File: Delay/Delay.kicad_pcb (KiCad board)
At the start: 2 copper layers, 63 parts, among them J1 9V battery, J2 DC IN, J4 IN, J5 OUT, U1 PT2399, U2 LP2950-5.0_TO252, U3 TL072

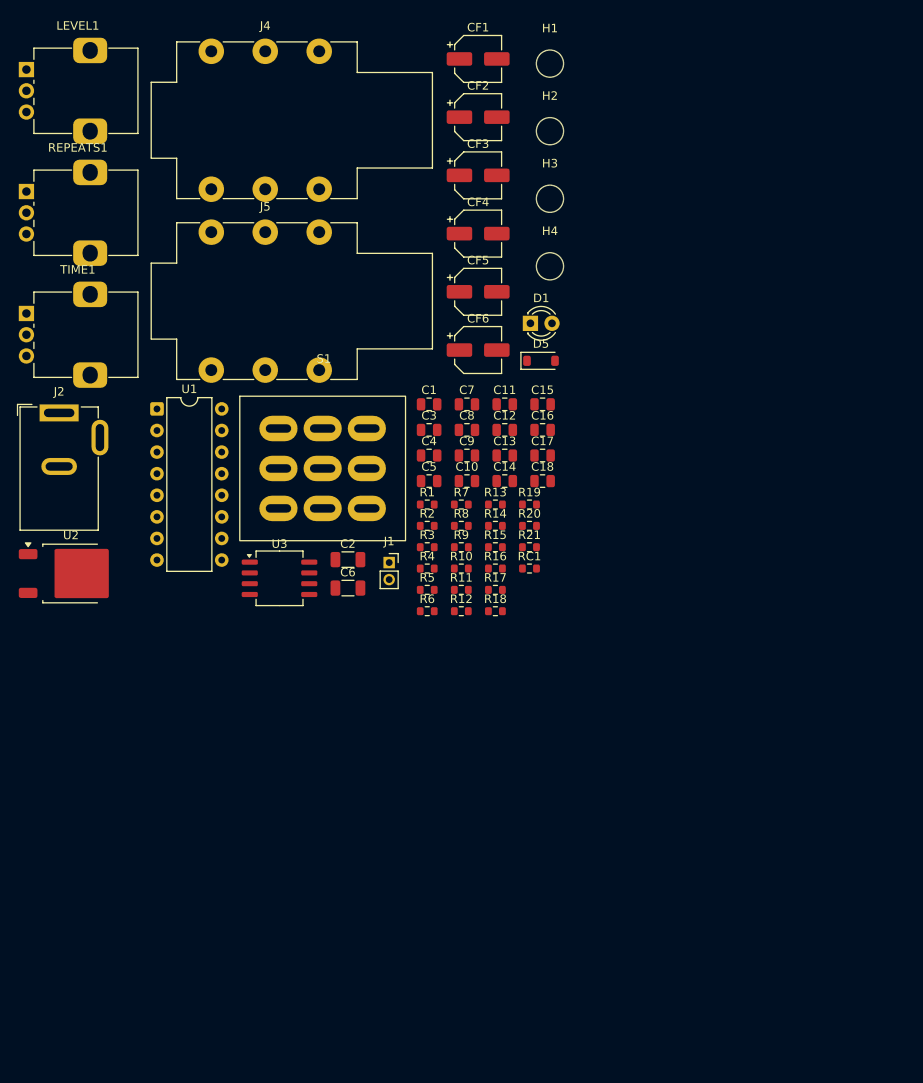
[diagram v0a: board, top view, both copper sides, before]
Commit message: Completed PCB layout, still need to finish BOM.
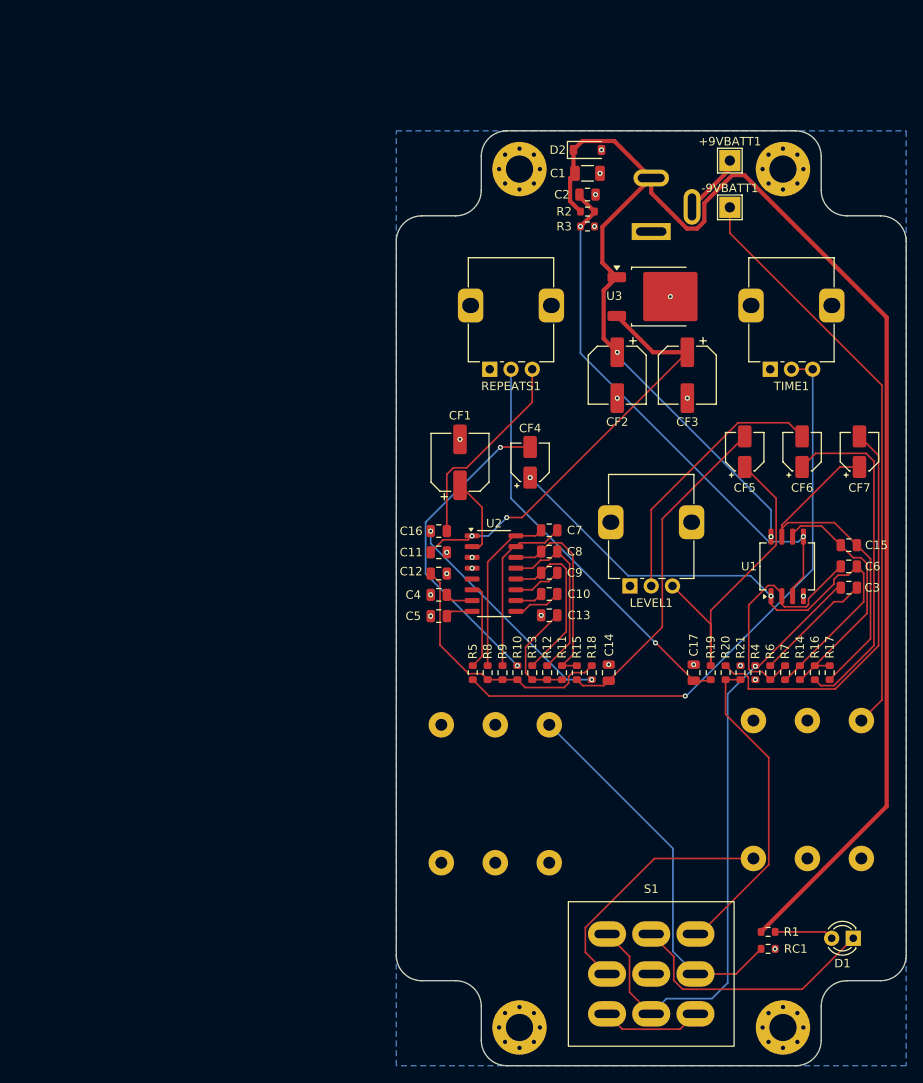
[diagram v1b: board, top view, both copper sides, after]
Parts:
- removed C18: 100pF, Capacitor_SMD:C_0805_2012Metric
- removed D5: 1N4148W, Diode_SMD:D_SOD-123
- removed J4: IN, Connector_Audio:Jack_6.35mm_Neutrik_NMJ6HFD2_Horizontal
- removed J5: OUT, Connector_Audio:Jack_6.35mm_Neutrik_NMJ6HFD2_Horizontal
- added +9VBATT1: 9V Batt +ve, TestPoint:TestPoint_THTPad_2.5x2.5mm_Drill1.2mm, F.Cu at (159.2, 43.5)
- added -9VBATT1: 9V Batt -ve, TestPoint:TestPoint_THTPad_2.5x2.5mm_Drill1.2mm, F.Cu at (159.2, 49.0)
- added CF7: 1uF, Capacitor_SMD:CP_Elec_4x5.4, F.Cu at (174.5, 77.8)
- added D2: 1N4148W, Diode_SMD:D_SOD-123, F.Cu at (142.5, 42.2)
- added J3: OUT, Connector_Audio:Jack_6.35mm_Neutrik_NMJ6HFD2_Horizontal, B.Cu at (138.0, 109.9)
- C1: value 100nF -> 100uF; footprint Capacitor_SMD:C_0805_2012Metric -> Capacitor_SMD:C_1206_3216Metric
- C11: value 10nF -> 100nF
- C12: value 10nF -> 4.7nF
- C13, C14: value 4.7nF -> 10nF
- C15: value 22nF -> 100pF
- C17: value 47pF -> 4.7nF
- C2: value 100uF -> 47uF; footprint Capacitor_SMD:C_1206_3216Metric -> Capacitor_SMD:C_0805_2012Metric
- C3: value 47uF -> 220nF
- C6: value 100uF -> 47pF; footprint Capacitor_SMD:C_1206_3216Metric -> Capacitor_SMD:C_0805_2012Metric
- C8: value 100nF -> 2.2nF
- C9: value 2.2nF -> 100nF
- CF1: footprint Capacitor_SMD:CP_Elec_5x3 -> Capacitor_SMD:CP_Elec_6.3x7.7
- CF2: value 1uF -> 100uF; footprint Capacitor_SMD:CP_Elec_5x3 -> Capacitor_SMD:CP_Elec_6.3x7.7
- CF3: value 1uF -> 47uF; footprint Capacitor_SMD:CP_Elec_5x3 -> Capacitor_SMD:CP_Elec_6.3x7.7
- CF4, CF6: footprint Capacitor_SMD:CP_Elec_5x3 -> Capacitor_SMD:CP_Elec_4x5.4
- CF5: value 47uF -> 1uF; footprint Capacitor_SMD:CP_Elec_5x3 -> Capacitor_SMD:CP_Elec_4x5.4
- H1, H2, H3, H4: footprint MountingHole:MountingHole_3.2mm_M3 -> MountingHole:MountingHole_3.2mm_M3_Pad_Via
- J1: value 9V battery -> IN; footprint Connector_PinSocket_2.00mm:PinSocket_1x02_P2.00mm_Vertical -> Connector_Audio:Jack_6.35mm_Neutrik_NMJ6HFD2_Horizontal; moved to B.Cu
- J2: moved to B.Cu
- R1: value 2.2k -> 470R
- R11: value 2k -> 20k
- R12: value 5.1k -> 10k
- R13: value 10R -> 10k
- R14: value 180k -> 22k
- R15: value 360k -> 1k
- R16: value 22k -> 20K
- R17: value 350R -> 12k
- R18: value 12k -> 5.1k
- R19: value 20K -> 2k
- R2: value 20k -> 10K
- R3: value 10k -> 10K
- R4: value 10K -> 1M
- R5: value 10K -> 2.2k
- R6: value 10k -> 220k
- R7: value 1k -> 470k
- U1: value PT2399 -> TL072; footprint Package_DIP:DIP-16_W7.62mm -> Package_SO:SOIC-8_5.3x6.2mm_P1.27mm
- U2: value LP2950-5.0_TO252 -> PT2399; footprint Package_TO_SOT_SMD:TO-252-2 -> Package_SO:SO-16_3.9x9.9mm_P1.27mm
- U3: value TL072 -> LP2950-5.0_TO252; footprint Package_SO:SOIC-8_5.3x6.2mm_P1.27mm -> Package_TO_SOT_SMD:TO-252-2
- moved H1 116.7 mm to (165.5, 145.5)
- moved LEVEL1 93.5 mm to (147.5, 93.5), turned to 90 degrees
- moved H4 89.6 mm to (134.5, 145.5)
- moved TIME1 87.8 mm to (164.0, 68.0), turned to 90 degrees
- moved D1 81.7 mm to (173.8, 135.0), turned to 180 degrees
- moved S1 77.7 mm to (150.0, 139.2)
- moved U1 76.4 mm to (166.0, 91.2), turned to 90 degrees
- moved J2 72.9 mm to (150.0, 51.9)
- moved R1 64.3 mm to (163.8, 134.2), turned to 180 degrees
- moved C6 59.0 mm to (173.2, 91.2)
- moved REPEATS1 58.4 mm to (131.0, 68.0), turned to 90 degrees
- moved U3 55.7 mm to (151.0, 59.5)
- moved J1 55.2 mm to (162.0, 125.6)
- moved RC1 52.8 mm to (163.8, 136.2)
- moved C3 52.8 mm to (173.2, 93.8)
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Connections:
- C1 pad 1: Net-(U1-CC0) -> +9V
- C10 pad 1: Net-(U1-OP1-IN) -> Net-(U2-OP1-IN)
- C10 pad 2: Net-(U1-OP1-OUT) -> Net-(U2-OP1-OUT)
- C11 pad 1: Net-(C11-Pad1) -> +5V
- C15 pad 1: Net-(C15-Pad1) -> Net-(U1B--)
- C16 pad 1: Wet In -> Net-(C16-Pad1)
- C17 pad 1: Net-(U3A--) -> Net-(C17-Pad1)
- C17 pad 2: Buffered Signal -> GND
- C2 pad 1: +9V -> +4.5V
- C3 pad 1: +4.5V -> Wet In
- C3 pad 2: GND -> Net-(C3-Pad2)
- C4 pad 1: Net-(U1-CC1) -> Net-(U2-CC1)
- C5 pad 1: +5V -> Net-(U2-CC0)
- C6 pad 1: +9V -> Net-(U1A--)
- C6 pad 2: GND -> Buffered Signal
- C7 pad 1: Net-(U1-LPF1-IN) -> Net-(U2-LPF1-IN)
- C7 pad 2: Net-(U1-LPF1-OUT) -> Net-(U2-LPF1-OUT)
- C8 pad 1: Net-(U1-OP2-OUT) -> Net-(U2-LPF2-OUT)
- C8 pad 2: Net-(U1-OP2-IN) -> Net-(U2-LPF2-IN)
- C9 pad 1: Net-(U1-LPF2-OUT) -> Net-(U2-OP2-OUT)
- C9 pad 2: Net-(U1-LPF2-IN) -> Net-(U2-OP2-IN)
- CF1 pad 1: Net-(U1-REF) -> Net-(U2-REF)
- CF2 pad 1: Net-(CF2-Pad1) -> +9V
- CF2 pad 2: Net-(C12-Pad1) -> GND
- CF3 pad 1: Buffered Signal -> +5V
- CF3 pad 2: Net-(CF3-Pad2) -> GND
- CF4 pad 1: Delayed Signal -> Buffered Signal
- CF5 pad 1: +5V -> Net-(CF5-Pad1)
- CF5 pad 2: GND -> Net-(C14-Pad1)
- CF6 pad 1: Net-(C18-Pad2) -> Delayed Signal
- J2 pad 3: /+ve -> Net-(+9VBATT1-Pad1)
- LEVEL1 pad 2: Net-(CF4-Pad2) -> Net-(CF6-Pad2)
- LEVEL1 pad 3: Net-(CF2-Pad1) -> Net-(CF5-Pad1)
- R1 pad 1: Net-(R1-Pad1) -> Net-(D1-A)
- R1 pad 2: Net-(U1-VCO) -> +9V
- R10 pad 1: Net-(CF3-Pad2) -> Net-(CF4-Pad2)
- R10 pad 2: Net-(C13-Pad1) -> Net-(C12-Pad1)
- R11 pad 1: Net-(C14-Pad1) -> Net-(C13-Pad1)
- R11 pad 2: Net-(CF2-Pad1) -> Net-(U2-LPF2-OUT)
- R12 pad 1: Net-(C15-Pad1) -> Net-(C13-Pad1)
- R12 pad 2: Net-(C13-Pad1) -> Net-(U2-LPF2-IN)
- R13 pad 1: GND -> Net-(C13-Pad1)
- R13 pad 2: Wet In -> Net-(U2-OP2-OUT)
- R14 pad 1: Net-(U3A--) -> Net-(U1B--)
- R14 pad 2: Net-(C16-Pad2) -> Buffered Signal
- R15 pad 1: Buffered Signal -> Net-(C14-Pad1)
- R15 pad 2: Net-(U3A--) -> Net-(U2-LPF2-OUT)
- R16 pad 1: Net-(U3B--) -> Net-(U1B--)
- R16 pad 2: Buffered Signal -> Delayed Signal
- R17 pad 1: Net-(D1-A) -> Net-(C15-Pad2)
- R17 pad 2: +9V -> Net-(U1B--)
- R18 pad 1: Net-(C18-Pad2) -> Net-(C16-Pad1)
- R18 pad 2: Net-(U3B--) -> Net-(C12-Pad1)
- R19 pad 1: Net-(U3B--) -> Net-(C17-Pad1)
- R19 pad 2: Delayed Signal -> Net-(CF5-Pad1)
- R2 pad 1: Net-(C11-Pad1) -> +9V
- R2 pad 2: Net-(U1-LPF2-OUT) -> +4.5V
- R20 pad 2: Net-(CF6-Pad2) -> Net-(CF7-Pad2)
- R3 pad 1: Net-(C11-Pad1) -> +4.5V
- R3 pad 2: Net-(U1-LPF2-IN) -> GND
- R4 pad 1: +9V -> GND
- R4 pad 2: +4.5V -> Wet In
- R5 pad 1: +4.5V -> Net-(R5-Pad1)
- R5 pad 2: GND -> Net-(U2-VCO)
- R6 pad 1: Net-(C11-Pad1) -> Net-(U1A--)
- R6 pad 2: Net-(U1-OP2-OUT) -> Net-(C3-Pad2)
- R7 pad 1: Net-(C12-Pad1) -> Buffered Signal
- R7 pad 2: Net-(U1-LPF2-OUT) -> Net-(U1A--)
- R8 pad 1: Net-(C13-Pad1) -> Net-(C12-Pad1)
- R8 pad 2: Net-(U1-LPF1-OUT) -> Net-(U2-LPF1-IN)
- R9 pad 1: Net-(C13-Pad1) -> Net-(C12-Pad1)
- R9 pad 2: Net-(U1-LPF1-IN) -> Net-(U2-LPF1-OUT)
- REPEATS1 pad 2: Net-(C14-Pad1) -> Net-(C17-Pad1)
- REPEATS1 pad 3: Net-(C15-Pad2) -> Net-(C16-Pad2)
- TIME1 pad 2: Net-(R1-Pad1) -> Net-(R5-Pad1)
- TIME1 pad 3: Net-(R1-Pad1) -> Net-(R5-Pad1)
- U1 pad 1: +5V -> Buffered Signal
- U1 pad 2: Net-(U1-REF) -> Net-(U1A--)
- U1 pad 3: GND -> +4.5V
- U1 pad 5: unconnected-(U1-CLK_O-Pad5) -> +4.5V
- U1 pad 6: Net-(U1-VCO) -> Net-(U1B--)
- U1 pad 7: Net-(U1-CC1) -> Net-(C15-Pad2)
- U1 pad 8: Net-(U1-CC0) -> +9V
- U2 pad 1: +9V -> +5V
- U2 pad 2: GND -> Net-(U2-REF)
- U2 pad 3: +5V -> GND
- U3 pad 1: Buffered Signal -> +9V
- U3 pad 2: Net-(U3A--) -> GND
- U3 pad 3: +4.5V -> +5V
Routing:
- net +9V: track 0.00 -> 193.7 mm, vias 0 -> 2
- net Wet In: track 0.00 -> 74.1 mm, vias 0 -> 1
- net Net-(R5-Pad1): track 0.00 -> 73.0 mm, vias 0 -> 1
- net Net-(-9VBATT1-Pad1): track 0.00 -> 68.8 mm
- net Buffered Signal: track 0.00 -> 65.4 mm, vias 0 -> 2
- net +4.5V: track 0.00 -> 63.0 mm, vias 0 -> 2
- net +5V: track 0.00 -> 50.0 mm, vias 0 -> 2
- net Net-(CF7-Pad2): track 0.00 -> 47.6 mm
- net Net-(C17-Pad1): track 0.00 -> 47.5 mm, vias 0 -> 1
- net Guitar Out: track 0.00 -> 45.4 mm
- net Net-(C15-Pad2): track 0.00 -> 43.0 mm
- net Delayed Signal: track 0.00 -> 40.4 mm
- net Net-(C14-Pad1): track 0.00 -> 39.7 mm
- net Net-(CF5-Pad1): track 0.00 -> 39.3 mm
- net Net-(CF4-Pad2): track 0.00 -> 37.3 mm, vias 0 -> 2
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- added copper zone on B.Cu, net GND
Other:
- board outline added: 60 x 110 mm

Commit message: Finalised PCB layout (110mmx60mm) and completed BOM (apart from C1 is only rated for 6.3V which might need to change).
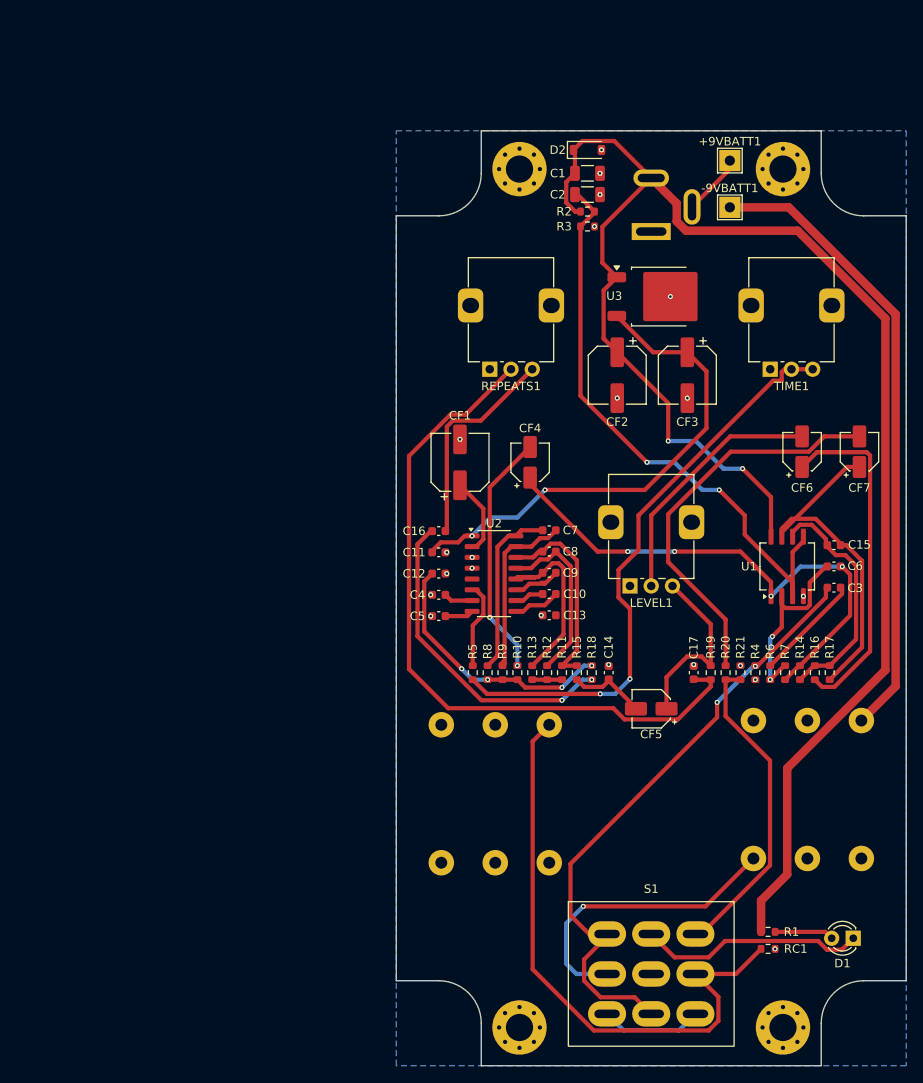
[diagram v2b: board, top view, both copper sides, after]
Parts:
- C10, C11, C12, C13, C14, C15, C16, C17, C3, C4, C5, C6, C7, C8, C9: footprint Capacitor_SMD:C_0805_2012Metric -> Capacitor_SMD:C_0603_1608Metric
- C2: footprint Capacitor_SMD:C_0805_2012Metric -> Capacitor_SMD:C_1206_3216Metric
- moved CF5 32.2 mm to (150.0, 108.0), turned to 180 degrees
- moved C15 1.75 mm to (171.5, 88.8)
- moved C3 1.75 mm to (171.5, 93.8)
- moved C6 1.75 mm to (171.5, 91.2)
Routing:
- net Net-(C17-Pad1): track 47.5 -> 85.4 mm, vias 1 -> 0
- net Net-(C14-Pad1): track 39.7 -> 8.93 mm
- net Guitar Out: track 45.4 -> 70.5 mm
- net Net-(CF5-Pad1): track 39.3 -> 21.6 mm
- net Net-(C16-Pad1): track 27.0 -> 37.6 mm
- net Net-(C13-Pad1): track 12.9 -> 3.50 mm
- net +5V: track 50.0 -> 58.4 mm
- net Delayed Signal: track 40.4 -> 48.7 mm
- net Net-(CF4-Pad2): track 37.3 -> 29.0 mm
- net +4.5V: track 63.0 -> 69.1 mm
- net Net-(U2-LPF2-IN): track 20.8 -> 26.5 mm
- net Guitar In: track 29.6 -> 35.2 mm, vias 0 -> 1
- net Net-(-9VBATT1-Pad1): track 68.8 -> 74.2 mm
- net Net-(U2-OP2-OUT): track 19.9 -> 25.0 mm
- net Net-(U2-OP1-OUT): track 5.72 -> 10.4 mm
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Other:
- outline, holes or cut-outs redrawn
